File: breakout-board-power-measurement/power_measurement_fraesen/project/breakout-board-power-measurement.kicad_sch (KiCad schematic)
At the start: 83 parts, among them J1 Screw_Terminal_01x04, J2 Conn_01x09, J3 Conn_01x07, J4 Conn_01x02, U1 MCP3911A0-E-SS, U2 Si8641BA-B-IU, U3 LM317_TO-252, Y1 10M

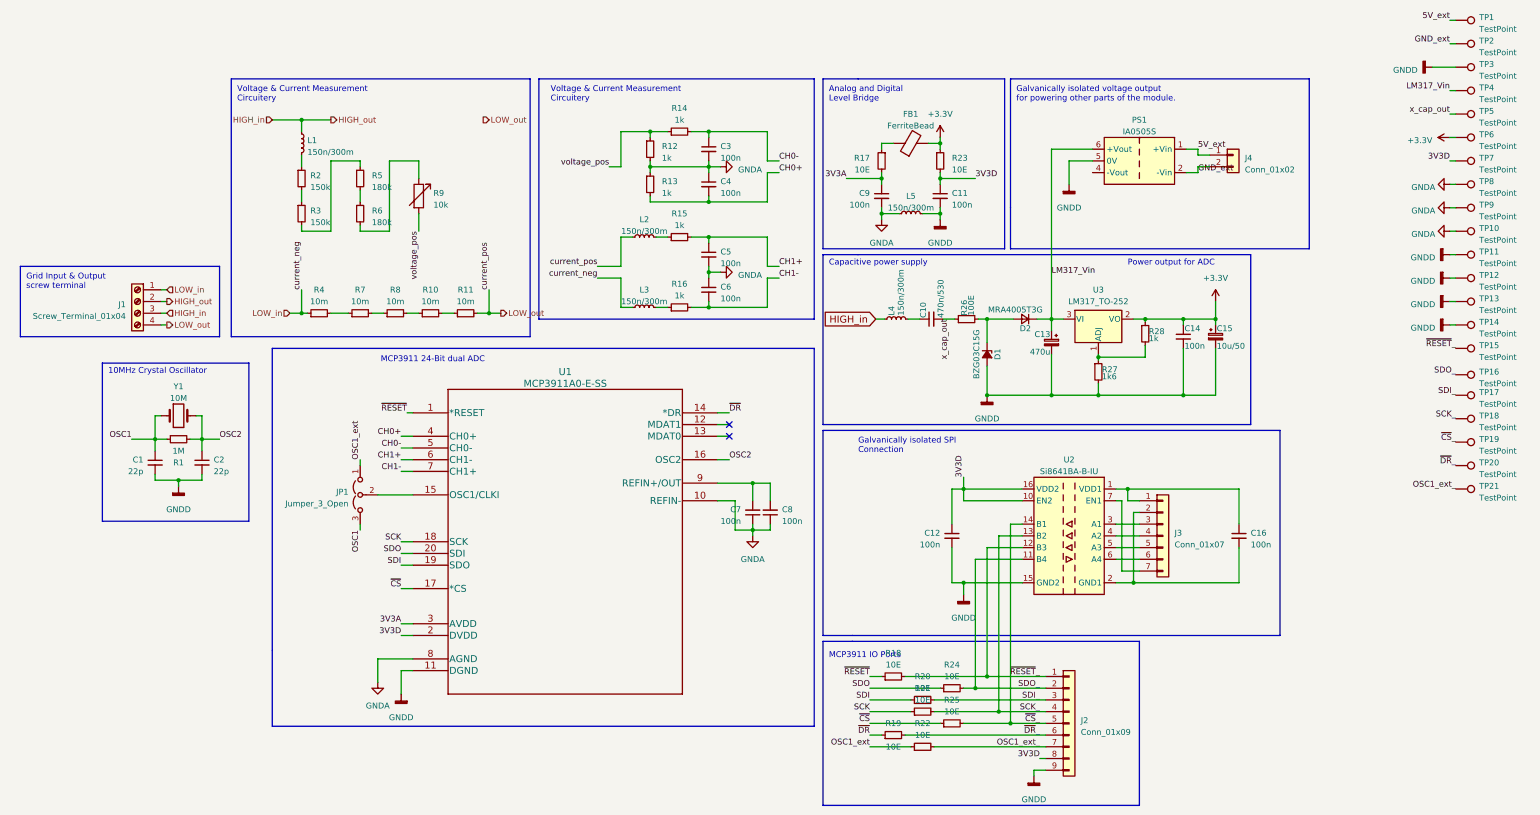
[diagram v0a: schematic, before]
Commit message: power measurement fertig fürs fräsen
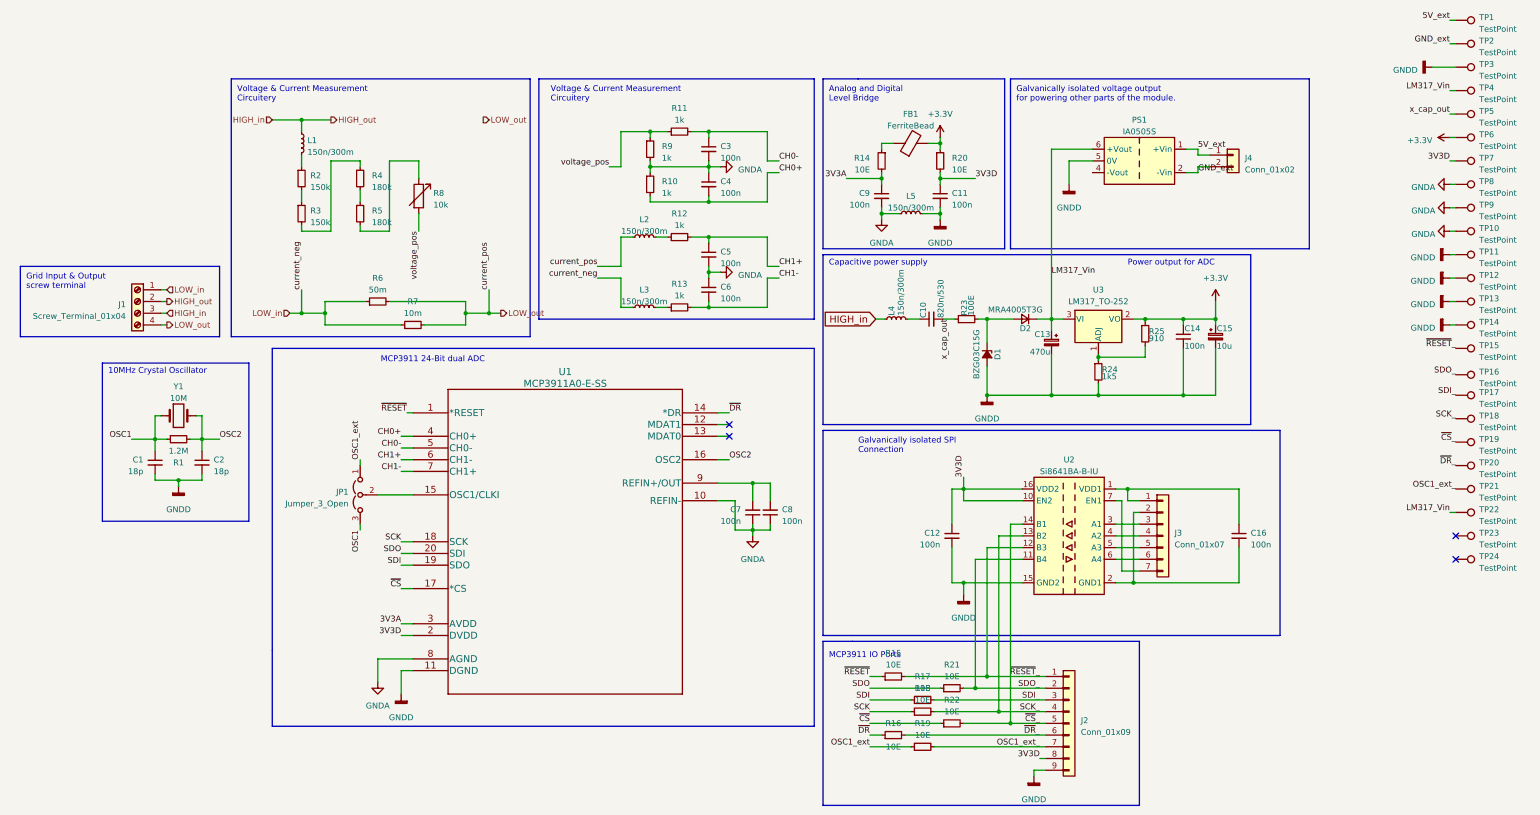
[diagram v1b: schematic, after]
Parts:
- removed R11, R4, R8: 10m, Resistor_SMD:R_1210_3225Metric, symbol Device:R_Small
- added TP22: TestPoint, Via:Via_THTPad_D1.5mm_Drill0.8mm, symbol Connector:TestPoint
- added TP23, TP24: TestPoint, Screwhole:Screwhole_THTPad_D3.0mm_Drill2.0mm, symbol Connector:TestPoint
- C1, C2: value 22p -> 18p; footprint Capacitor_SMD:C_1206_3216Metric_Pad1.33x1.80mm_HandSolder -> Capacitor_SMD:C_0805_2012Metric_Pad1.18x1.45mm_HandSolder
- C10: value 470n/530 -> 820n/530
- C13: footprint Capacitor_Tantalum_SMD:CP_EIA-7343-31_Kemet-D_Pad2.25x2.55mm_HandSolder -> Capacitor_THT:CP_Radial_D10.0mm_P5.00mm
- C15: value 10u/50 -> 10u; footprint Capacitor_Tantalum_SMD:CP_EIA-7343-31_Kemet-D_Pad2.25x2.55mm_HandSolder -> Capacitor_SMD:C_1206_3216Metric_Pad1.33x1.80mm_HandSolder
- D2: footprint Diode_SMD:D_SMA-SMB_Universal_Handsoldering -> Diode_SMD:D_MicroMELF_Handsoldering
- FB1: footprint Diode_SMD:D_SMA-SMB_Universal_Handsoldering -> Inductor_SMD:L_1210_3225Metric_Pad1.42x2.65mm_HandSolder
- R1: value 1M -> 1.2M
- R14: renamed from R17; footprint Resistor_SMD:R_1206_3216Metric_Pad1.30x1.75mm_HandSolder -> Resistor_SMD:R_0805_2012Metric_Pad1.20x1.40mm_HandSolder
- R15: renamed from R18; footprint Resistor_SMD:R_1206_3216Metric_Pad1.30x1.75mm_HandSolder -> Resistor_SMD:R_0805_2012Metric_Pad1.20x1.40mm_HandSolder
- R16: renamed from R19; footprint Resistor_SMD:R_1206_3216Metric_Pad1.30x1.75mm_HandSolder -> Resistor_SMD:R_0805_2012Metric_Pad1.20x1.40mm_HandSolder
- R17: renamed from R20; footprint Resistor_SMD:R_1206_3216Metric_Pad1.30x1.75mm_HandSolder -> Resistor_SMD:R_0805_2012Metric_Pad1.20x1.40mm_HandSolder
- R18: renamed from R21; footprint Resistor_SMD:R_1206_3216Metric_Pad1.30x1.75mm_HandSolder -> Resistor_SMD:R_0805_2012Metric_Pad1.20x1.40mm_HandSolder
- R19: renamed from R22; footprint Resistor_SMD:R_1206_3216Metric_Pad1.30x1.75mm_HandSolder -> Resistor_SMD:R_0805_2012Metric_Pad1.20x1.40mm_HandSolder
- R20: renamed from R23; footprint Resistor_SMD:R_1206_3216Metric_Pad1.30x1.75mm_HandSolder -> Resistor_SMD:R_0805_2012Metric_Pad1.20x1.40mm_HandSolder
- R21: renamed from R24; footprint Resistor_SMD:R_1206_3216Metric_Pad1.30x1.75mm_HandSolder -> Resistor_SMD:R_0805_2012Metric_Pad1.20x1.40mm_HandSolder
- R22: renamed from R25; footprint Resistor_SMD:R_1206_3216Metric_Pad1.30x1.75mm_HandSolder -> Resistor_SMD:R_0805_2012Metric_Pad1.20x1.40mm_HandSolder
- R24: renamed from R27; value 1k6 -> 1k5
- R25: renamed from R28; value 1k -> 910
- R6: renamed from R7; value 10m -> 50m; footprint Resistor_SMD:R_1210_3225Metric -> Resistor_SMD:R_2512_6332Metric
- R7: renamed from R10; footprint Resistor_SMD:R_1210_3225Metric -> Resistor_SMD:R_2512_6332Metric
- TP1, TP10, TP11, TP12, TP13, TP14, TP15, TP16, TP17, TP18, TP19, TP2, TP20, TP21, TP3, TP4, TP5, TP6, TP7, TP8, TP9: footprint TestPoint:TestPoint_THTPad_D1.0mm_Drill0.5mm -> Via:Via_THTPad_D1.5mm_Drill0.8mm
- renumbered R13 to R10, R14 to R11, R15 to R12, R16 to R13, R26 to R23, R5 to R4, R6 to R5, R9 to R8, R12 to R9
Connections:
- net LM317_Vin: now also TP22.1
- net LOW_in: now also R6.1, R7.1
- net LOW_out: now also R6.2, R7.2
- no-connect marks 2 -> 4
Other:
- moved on the sheet: R6, R7
